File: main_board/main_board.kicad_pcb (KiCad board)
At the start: 2 copper layers, 34 parts, among them J1 ESP32_LEFT, J10 +VB, J11 -VB, J12 USB_C, J2 ESP32_RIGHT, J3 Conn_01x08, J4 Battery Lipo 3,7v, J5 SD_CARD, J6 DD0503MB Module, J8 VIN_C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

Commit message: update PCB -- finish routing pcb
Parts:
- added REF**: MountingHole_3mm, MountingHole:MountingHole_3mm, F.Cu at (193.5, 52.3)
- added REF**: MountingHole_3mm, MountingHole:MountingHole_3mm, F.Cu at (182.1, 153.2)
- added REF**: MountingHole_3mm, MountingHole:MountingHole_3mm, F.Cu at (113.3, 154.2)
- added REF**: MountingHole_3mm, MountingHole:MountingHole_3mm, F.Cu at (103.1, 52.8)
- D2: value LED -> LED 1
- D3: value LED -> LED 2
- J1, J10, J11, J2, J5, J8, J9: moved to B.Cu
- J3: value Conn_01x08 -> LCD
- moved SW_RIGHT1 119.7 mm to (118.2, 129.8)
- moved SW_DOWN1 119.0 mm to (108.0, 140.0)
- moved SW_UP1 116.3 mm to (108.7, 119.7)
- moved SW_LEFT1 115.0 mm to (97.8, 129.8)
- moved R8 108.4 mm to (163.3, 119.1), turned to 90 degrees
- moved R3 103.5 mm to (153.6, 142.2), turned to 180 degrees
- moved ON/OFF1 100.9 mm to (159.6, 142.2)
- moved R9 91.5 mm to (146.1, 119.6), turned to 90 degrees
- moved D3 89.4 mm to (124.6, 69.3)
- moved R1 88.1 mm to (119.5, 69.3), turned to 180 degrees
- moved SW_B1 87.9 mm to (149.6, 117.9)
- moved SW_A1 87.6 mm to (167.4, 117.9)
- moved R2 86.2 mm to (119.5, 75.4), turned to 180 degrees
- moved R11 84.7 mm to (139.8, 141.0)
- moved D2 83.1 mm to (124.6, 75.4)
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- renumbered D1 to ON/OFF1
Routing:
- net GPIO47: track 0.00 -> 158.0 mm
- net GPIO21: track 0.00 -> 132.0 mm
- net GPIO11: track 0.00 -> 78.1 mm
- net GPIO18: track 0.00 -> 76.7 mm
- net GPIO4: track 0.00 -> 71.5 mm
- net GPIO5: track 0.00 -> 64.4 mm
- net GPIO12: track 0.00 -> 62.1 mm
- net Vout_reg: track 0.00 -> 57.3 mm
- net GPIO16: track 0.00 -> 53.7 mm
- net GPIO15: track 0.00 -> 40.6 mm
- net GPIO17: track 0.00 -> 40.1 mm
- net +Vb: track 0.00 -> 29.0 mm
- net GPIO6: track 0.00 -> 28.6 mm
- net GPIO9: track 0.00 -> 27.2 mm
- net -Vb: track 0.00 -> 26.9 mm, vias 0 -> 1
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- added copper zone on In1.Cu, net +3.3V
- added copper zone on In2.Cu, net -Vb
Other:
- board outline added: 122.4 x 120.1 mm
- copper layers 2 -> 4
- board text added: "ESP32"
- board text added: "GAMEBOY -- YOUSSOUF & ISMAIL"
- board text added: "SCREEN"
- board text added: "SD CARD"

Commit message: Version 1 PCB finished
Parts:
- moved SW_B1 22.8 mm to (170.3, 127.6)
- moved R9 20.8 mm to (165.1, 127.9)
- moved SW_A1 19.1 mm to (186.3, 120.7)
- moved R8 14.0 mm to (177.3, 119.9)
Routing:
- net GPIO5: track 64.4 -> 96.3 mm
- net GPIO6: track 28.6 -> 54.9 mm
- net GPIO47: track 158.0 -> 178.4 mm
- net GPIO21: track 132.0 -> 150.6 mm
- net -Vb: track 26.9 -> 20.4 mm

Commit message: pcb version 2 PCB mode
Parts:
- removed REF** (x4): MountingHole_3mm, MountingHole:MountingHole_3mm
- moved R1 65.9 mm to (136.0, 133.1), turned to 0 degrees
- moved D3 59.8 mm to (136.0, 128.0), turned to 180 degrees
- moved R2 58.5 mm to (129.4, 133.1), turned to 0 degrees
- moved J4 57.1 mm to (98.6, 127.5), turned to 90 degrees
- moved J5 55.1 mm to (174.2, 145.8), turned to -90 degrees
- moved D2 52.4 mm to (126.6, 127.8), turned to 180 degrees
- moved SW1 51.5 mm to (68.3, 125.5)
- moved J10 50.2 mm to (88.6, 131.1), turned to 180 degrees
- moved J11 44.8 mm to (88.6, 120.9), turned to 180 degrees
- moved R5 44.6 mm to (76.6, 107.7)
- moved R4 44.0 mm to (68.9, 93.8)
- moved SW_RIGHT1 44.0 mm to (83.4, 102.9)
- moved SW_UP1 44.0 mm to (74.0, 92.7)
- moved R6 44.0 mm to (95.6, 102.8)
- moved SW_DOWN1 44.0 mm to (73.3, 113.0)
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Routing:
- net GPIO47: track 178.4 -> 53.1 mm
- net GPIO21: track 150.6 -> 37.4 mm
- net GPIO11: track 78.1 -> 138.9 mm
- net GPIO12: track 62.1 -> 122.5 mm
- net Vout_reg: track 57.3 -> 13.4 mm
- net GPIO9: track 27.2 -> 70.1 mm
- net GPIO18: track 76.7 -> 115.0 mm
- net GPIO16: track 53.7 -> 90.4 mm
- net GPIO13: track 21.2 -> 57.5 mm
- net GPIO4: track 71.5 -> 106.0 mm
- net GPIO6: track 54.9 -> 88.9 mm
- net GPIO15: track 40.6 -> 73.8 mm
- net GPIO17: track 40.1 -> 72.2 mm
- net +3.3V: track 17.8 -> 44.9 mm, vias 9 -> 6
- net GPIO5: track 96.3 -> 122.2 mm
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- added copper zone on In2.Cu, net +3.3V
- added copper zone on In1.Cu, net -Vb
- removed copper zone on In1.Cu, net +3.3V
- removed copper zone on In2.Cu, net -Vb
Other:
- board outline removed
- board text removed: "GAMEBOY -- YOUSSOUF & ISMAIL"

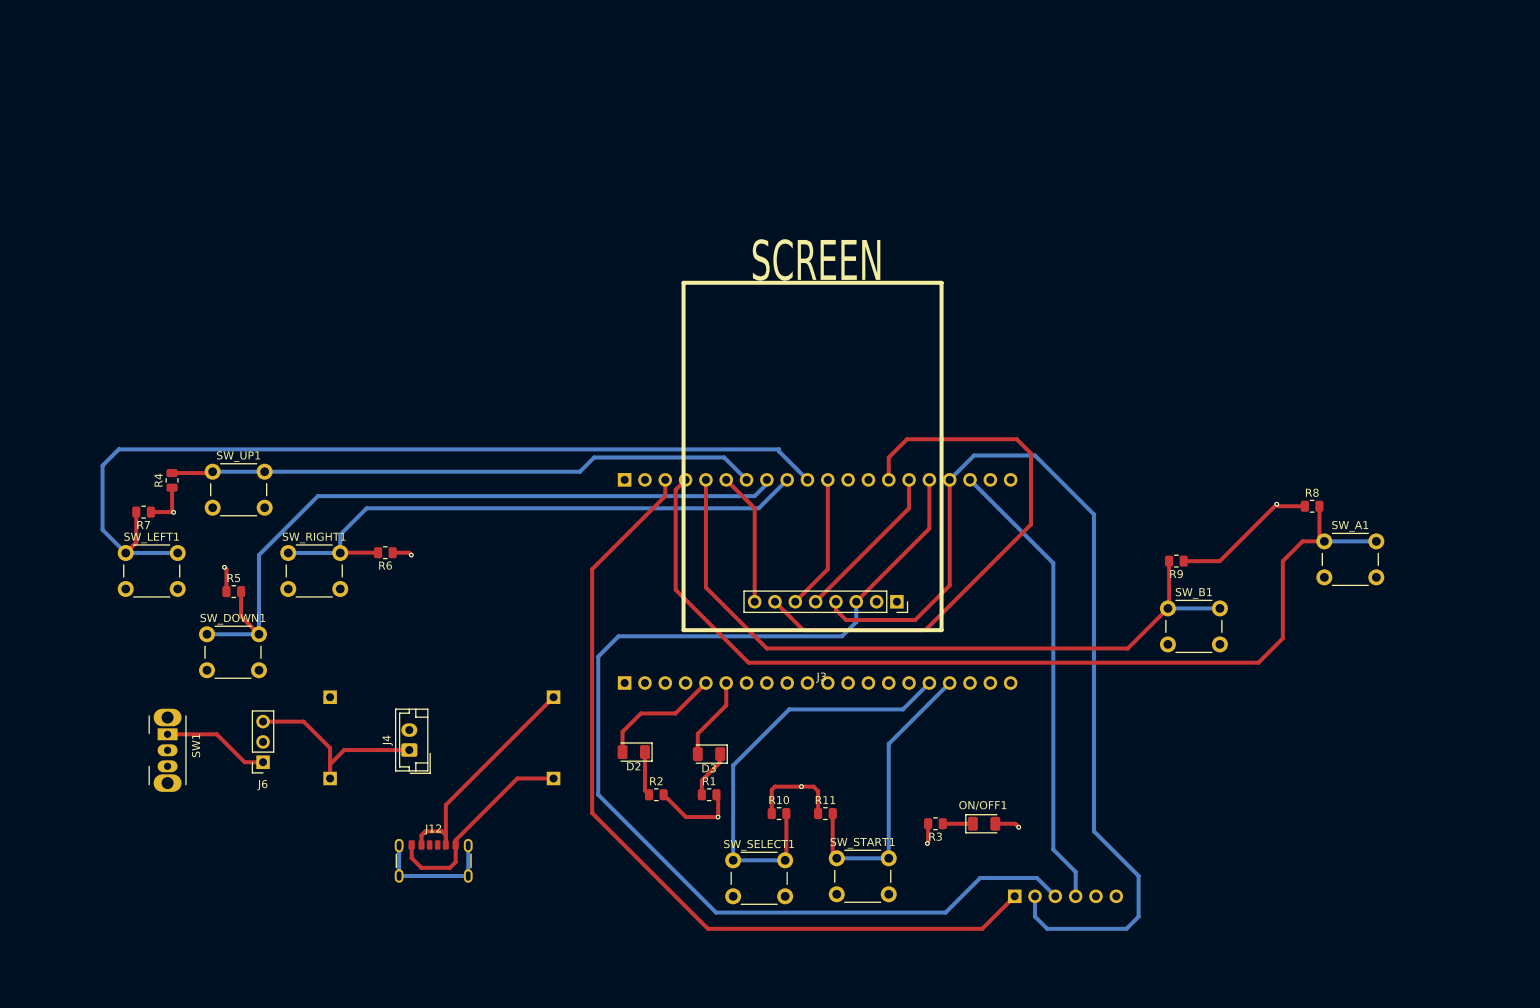
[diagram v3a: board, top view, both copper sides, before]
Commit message: change LCD , correct charger board footprint and PSP mode
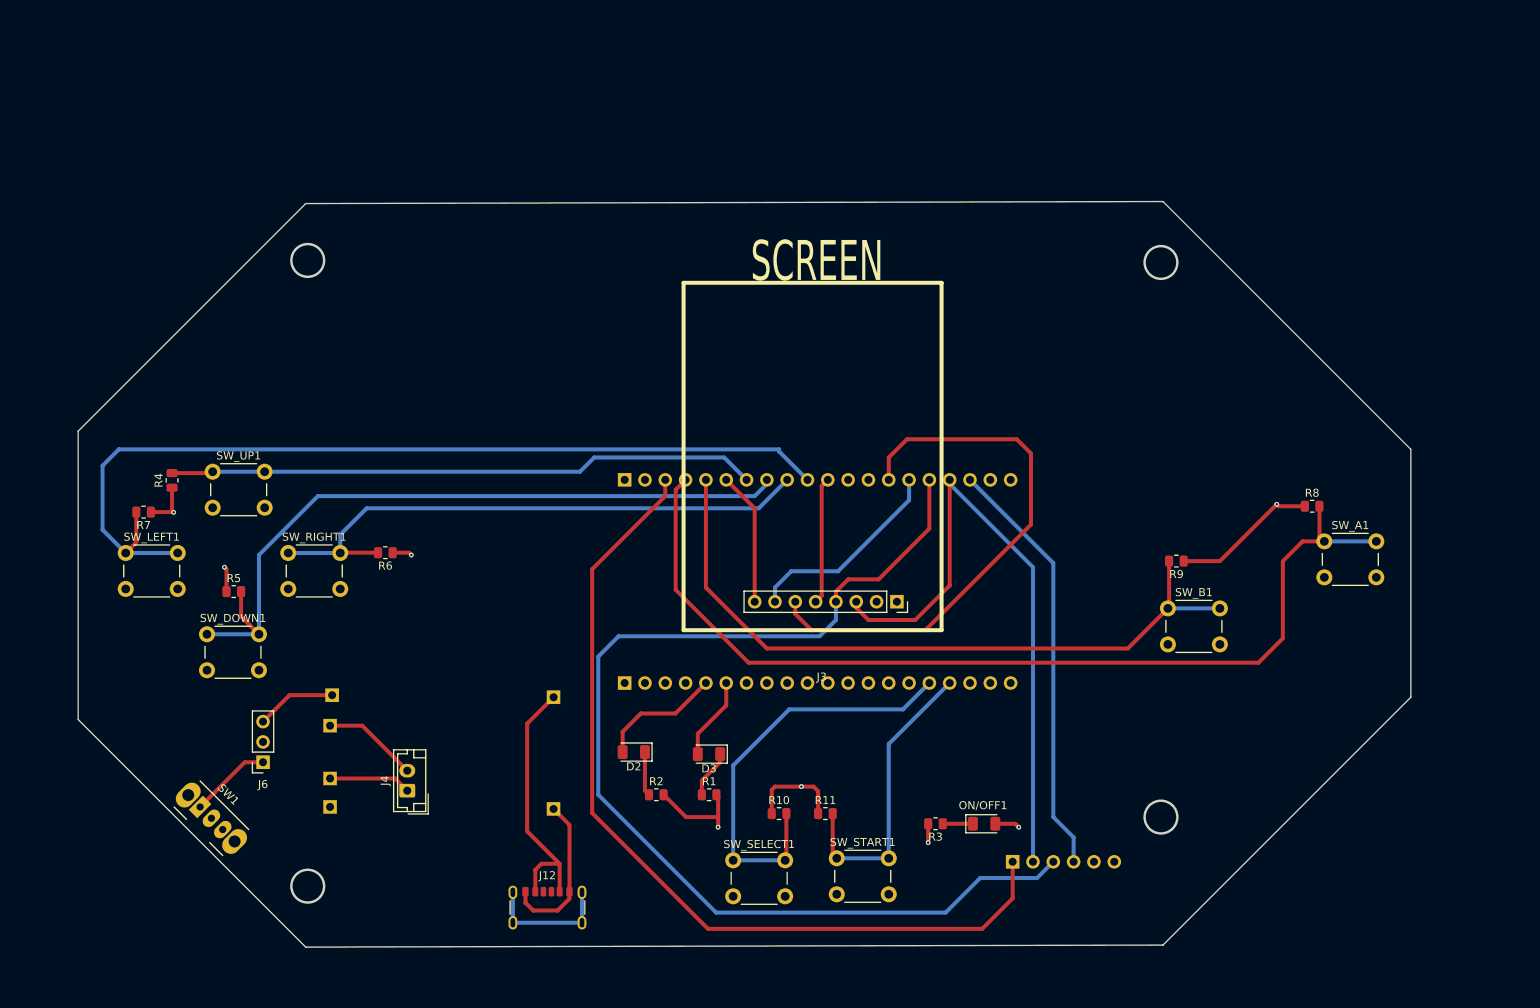
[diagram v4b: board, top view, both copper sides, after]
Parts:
- added J13: -Vout, Connector_PinHeader_2.54mm:PinHeader_1x01_P2.54mm_Vertical, B.Cu at (88.6, 134.6)
- added J7: +Vout, Connector_PinHeader_2.54mm:PinHeader_1x01_P2.54mm_Vertical, B.Cu at (88.9, 120.7)
- moved J12 15.4 mm to (115.8, 148.3)
- moved SW1 9.95 mm to (72.4, 134.6), turned to -45 degrees
- moved J4 5.09 mm to (98.3, 132.6)
- moved J5 4.33 mm to (174.0, 141.5)
- moved J9 3.81 mm to (116.6, 134.9)
- moved J11 3.56 mm to (88.6, 124.5)
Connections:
- J2 pad 20: -Vb -> Vout-
- J3 pad 1: +3.3V -> Vout-
- J3 pad 2: -Vb -> +3.3V
- J3 pad 3: GPIO11 -> GPIO12
- J3 pad 4: GPIO12 -> GPIO11
- J3 pad 5: GPIO10 -> GPIO8
- J3 pad 6: GPIO8 -> GPIO9
- J3 pad 7: GPIO9 -> GPIO10
- J5 pad 6: -Vb -> Vout-
- J6 pad 2: -Vb -> Vout-
- J6 pad 3: +Vb -> Vout+
- R1 pad 2: -Vb -> Vout-
- R2 pad 2: -Vb -> Vout-
- R3 pad 2: -Vb -> Vout-
- SW_A1 pad 2: -Vb -> Vout-
- SW_B1 pad 2: -Vb -> Vout-
- SW_DOWN1 pad 2: -Vb -> Vout-
- SW_LEFT1 pad 2: -Vb -> Vout-
- SW_RIGHT1 pad 2: -Vb -> Vout-
- SW_SELECT1 pad 2: -Vb -> Vout-
- SW_START1 pad 2: -Vb -> Vout-
- SW_UP1 pad 2: -Vb -> Vout-
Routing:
- net GPIO12: track 122.5 -> 80.1 mm
- net +Vb: track 26.0 -> 10.3 mm
- net Vout-: track 0.00 -> 14.5 mm, vias 0 -> 2
- net Vout+: track 0.00 -> 10.0 mm
- net -VIN_charge: track 26.1 -> 19.9 mm
- net GPIO10: track 20.1 -> 25.6 mm
- net GPIO13: track 57.5 -> 53.1 mm
- net GPIO4: track 106.0 -> 110.2 mm
- net +VIN_charge: track 29.9 -> 33.4 mm
- net Vout_reg: track 13.4 -> 10.2 mm
- net GPIO9: track 70.1 -> 68.4 mm
- net -Vb: track 13.4 -> 12.0 mm, vias 2 -> 0
- net GPIO8: track 16.9 -> 15.9 mm
- added copper zone on In1.Cu, net Vout-
- removed copper zone on In1.Cu, net -Vb
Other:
- board outline added: 166.6 x 93.2 mm
